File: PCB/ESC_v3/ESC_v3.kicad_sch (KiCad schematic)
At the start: 75 parts, among them J1 Conn_01x04_Pin, J11 Screw_Terminal_01x01, J2 Screw_Terminal_01x01, Q1 NTMFS2D1N08XT1G, Q2 NTMFS2D1N08XT1G, Q3 NTMFS2D1N08XT1G, Q4 NTMFS2D1N08XT1G, Q5 NTMFS2D1N08XT1G, Q6 NTMFS2D1N08XT1G, U1 SN65HVD232

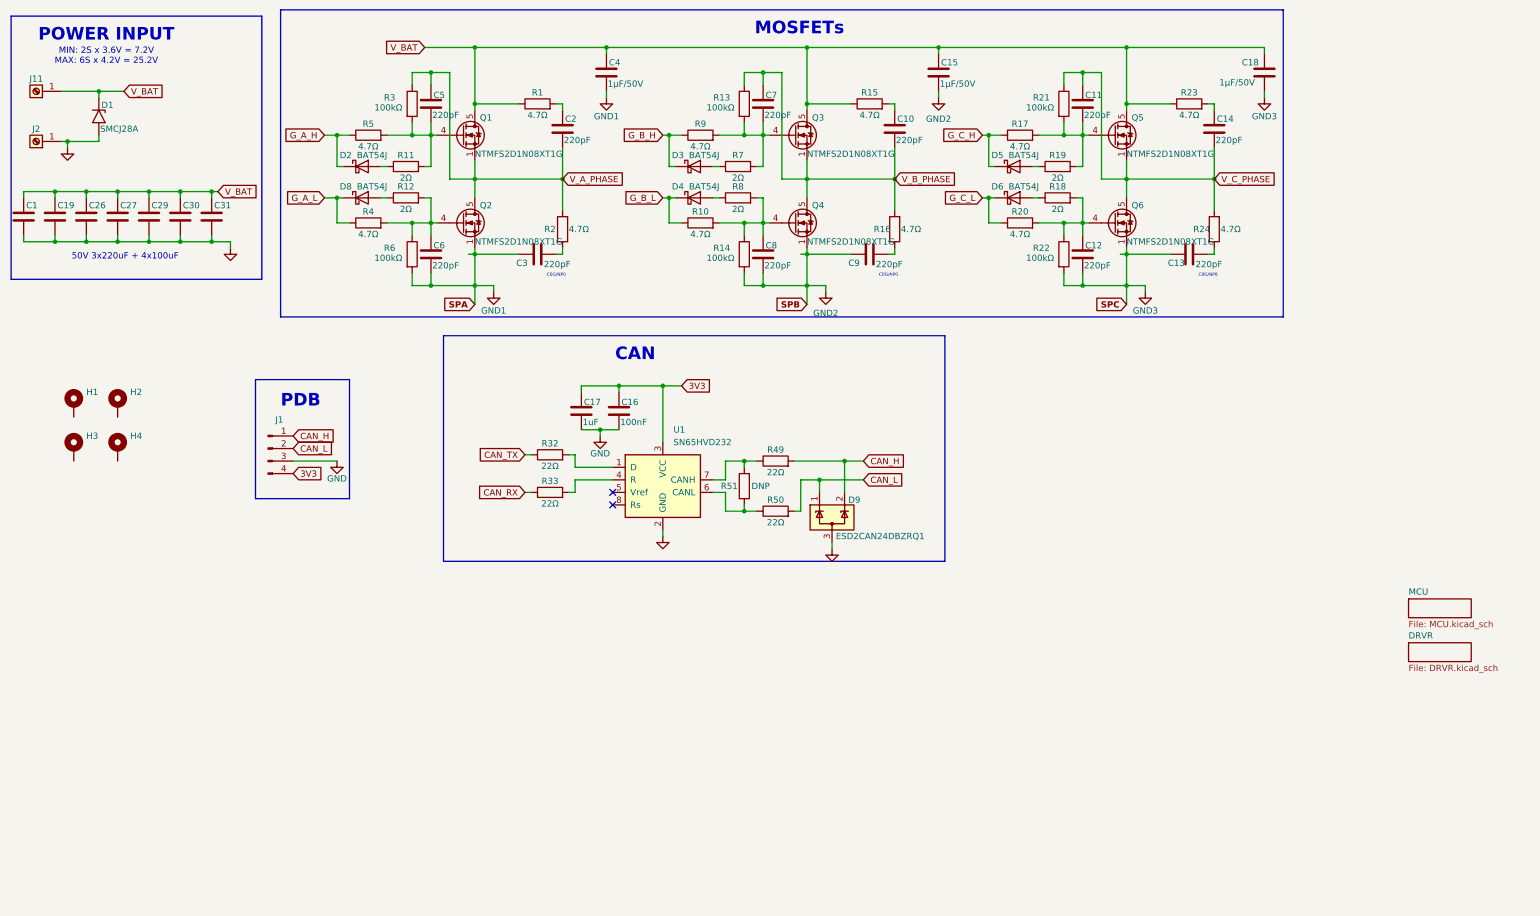
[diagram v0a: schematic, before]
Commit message: Update PCB layout and driver schematic
Adjust KiCad project files: many PCB footprint positions/rotations/uuids and silk/pad orientations updated, trace segments and widths adjusted, vias added/moved (several tented/free vias), and zone_connect enabled on referenced footprints. Correct MCU pin net assignments (PB4/PB5/PB6 / NFAULT / EN_DV) and other net fixes. In DRVR schematic change stroke styles to dashed and update a capacitor value from ">=10uF" to "22u". Remove several old backup zip files and add new backup snapshots. Miscellaneous small .kicad_prl/.kicad_sch/.ioc updates included for consistency and routing cleanup.
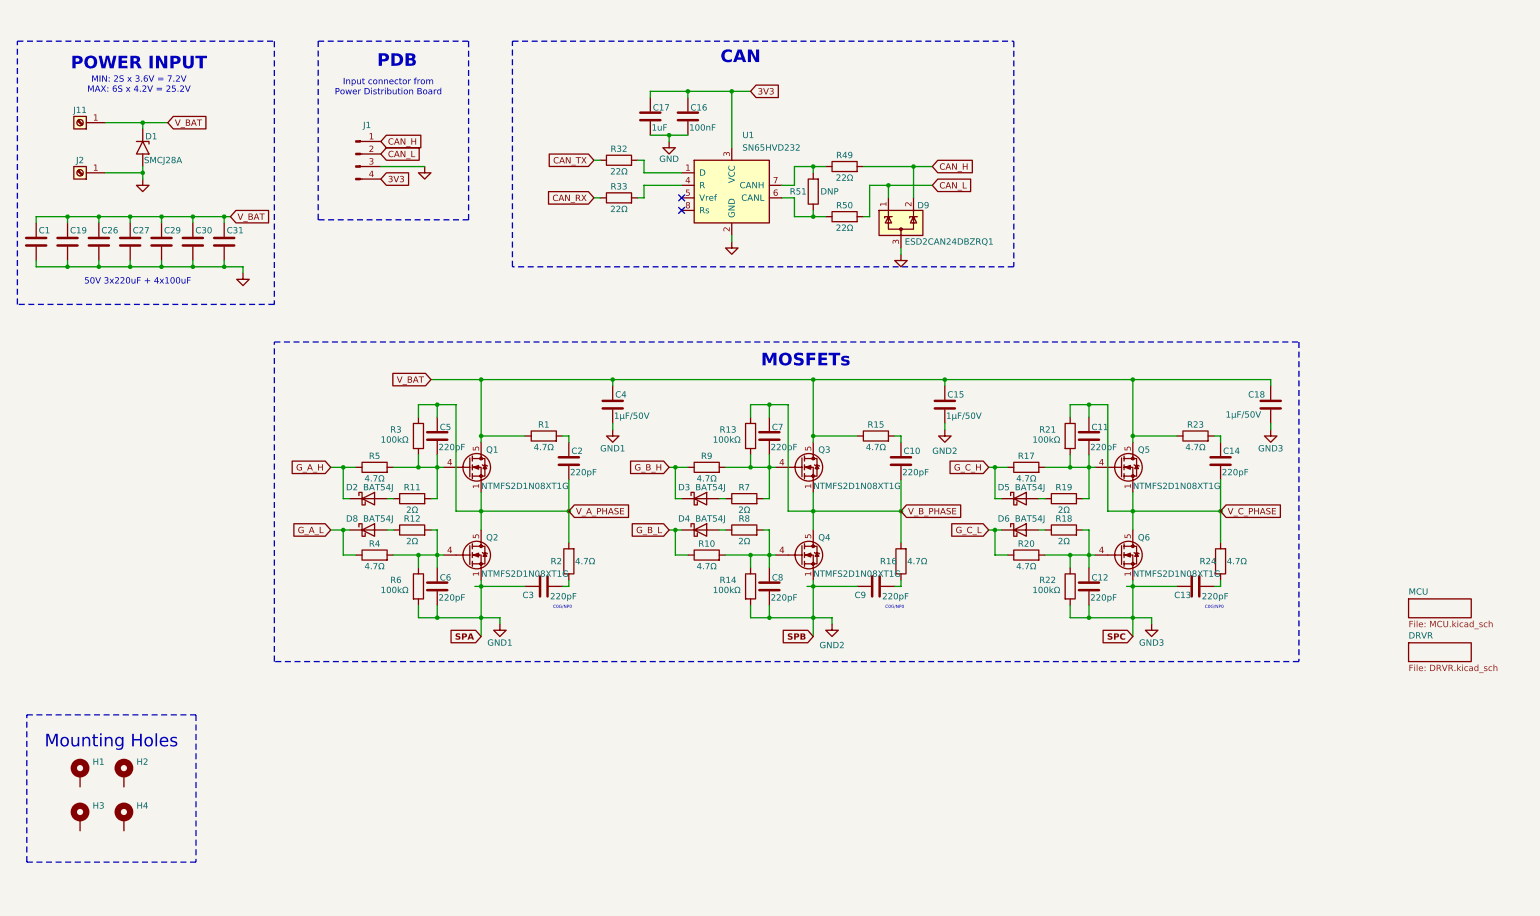
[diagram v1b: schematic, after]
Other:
- note added: "Input connector from Power Distribution Board"
- note added: "Mounting Holes"
- moved on the sheet: C1, C10, C11, C12, C13, C14, C15, C16, C17, C18, C19, C2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

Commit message: Reposition DRVR schematic elements
Adjust layout in PCB/ESC_v3/DRVR.kicad_sch: updated coordinates for rectangles, text labels, junctions, wires and pins to tidy and realign the driver schematic. Changes are graphical/coordinate-only (no netlist/electrical changes). Also touched project files (ESC_v3.*) and refreshed backup archives (deleted several older backups and added new snapshots).
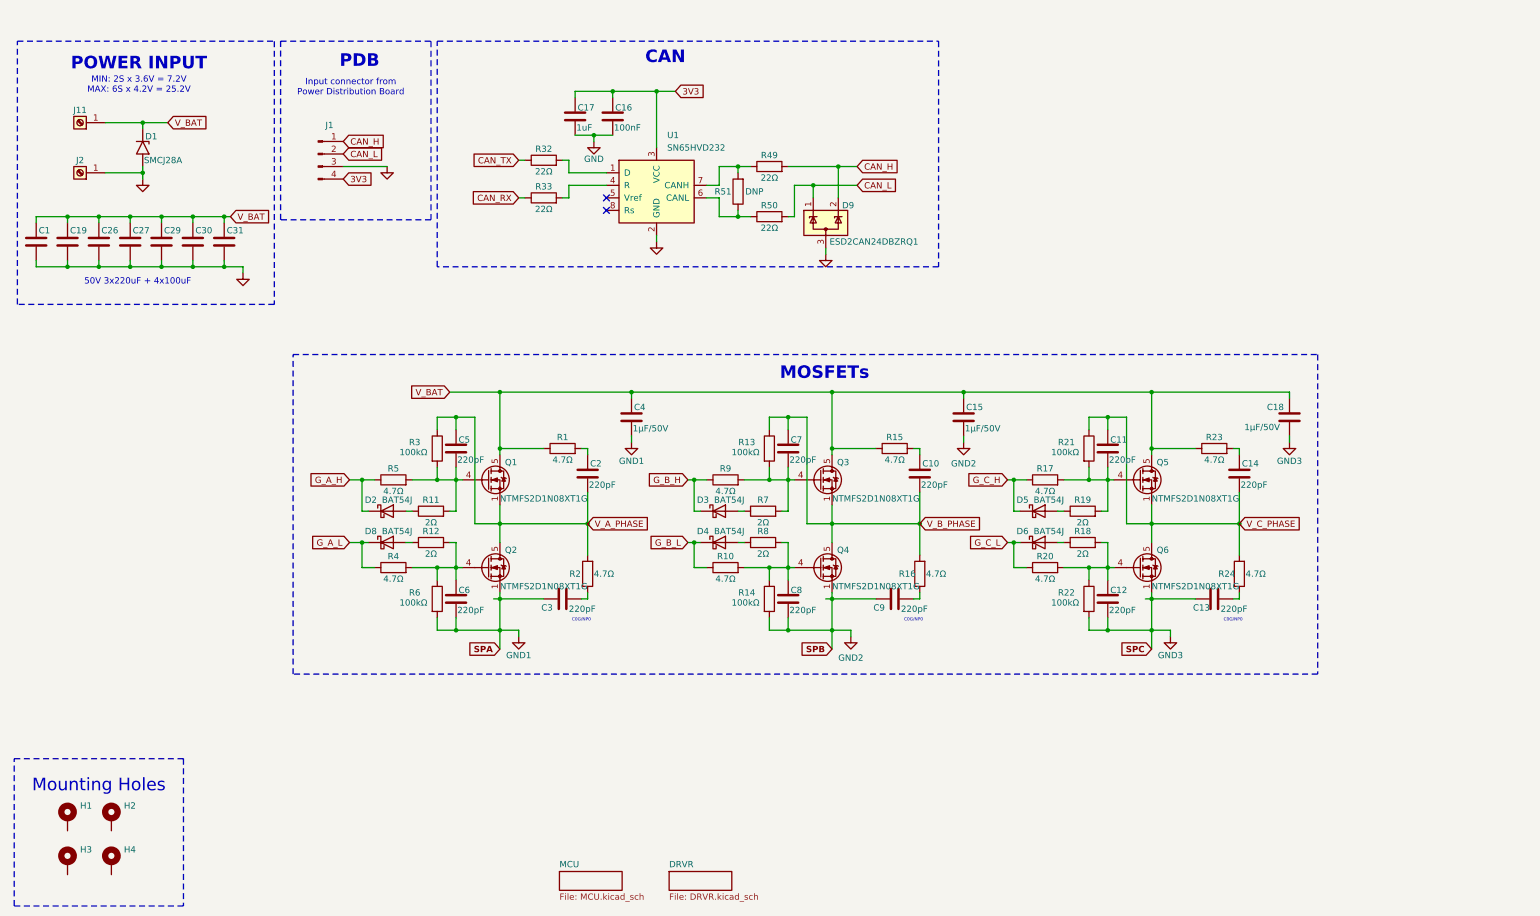
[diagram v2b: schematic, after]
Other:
- moved on the sheet: C10, C11, C12, C13, C14, C15, C16, C17, C18, C2, C3, C4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

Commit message: Update ESC_v3 schematics and PCB layout
Add net-tie symbol and +3V3/GND1 power symbols to DRVR schematic and reorganize schematic graphics (rectangles, text), junctions, and wires with updated coordinates/UUIDs. Also update top-level ESC_v3 schematic and MCU schematic along with PCB (.kicad_pcb) and panel (.kicad_prl) files. Remove several old backup zip files and add new backups for the ESC_v3 project.
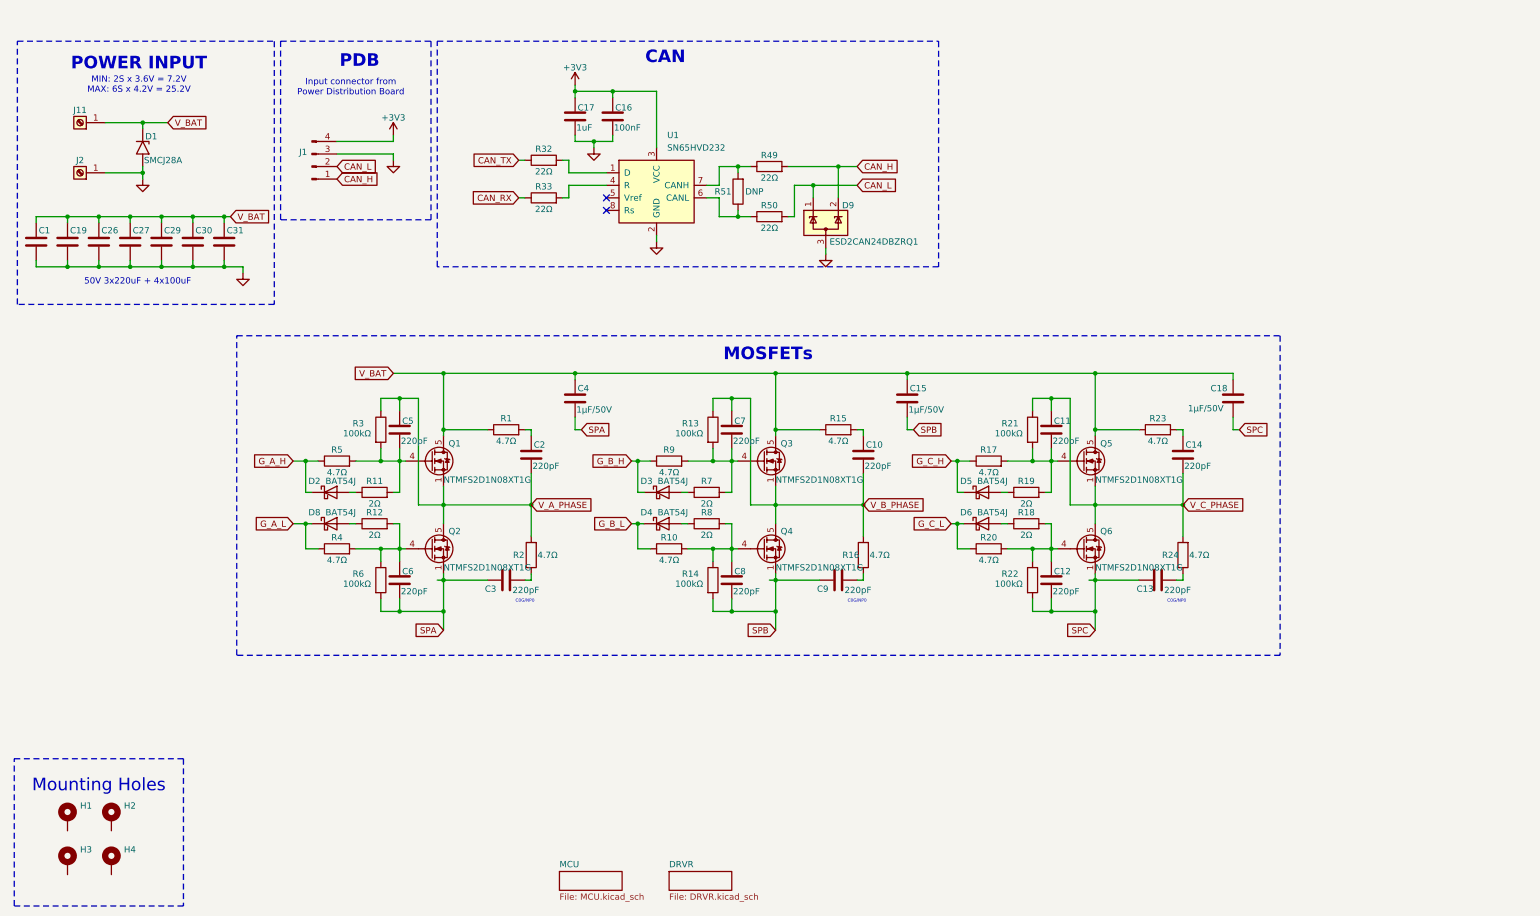
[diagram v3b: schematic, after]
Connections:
- net 3V3 renamed +3V3
- net GND1 renamed SPA
- net GND2 renamed SPB
- net GND3 renamed SPC
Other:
- moved on the sheet: C10, C11, C12, C13, C14, C15, C18, C2, C3, C4, C5, C6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

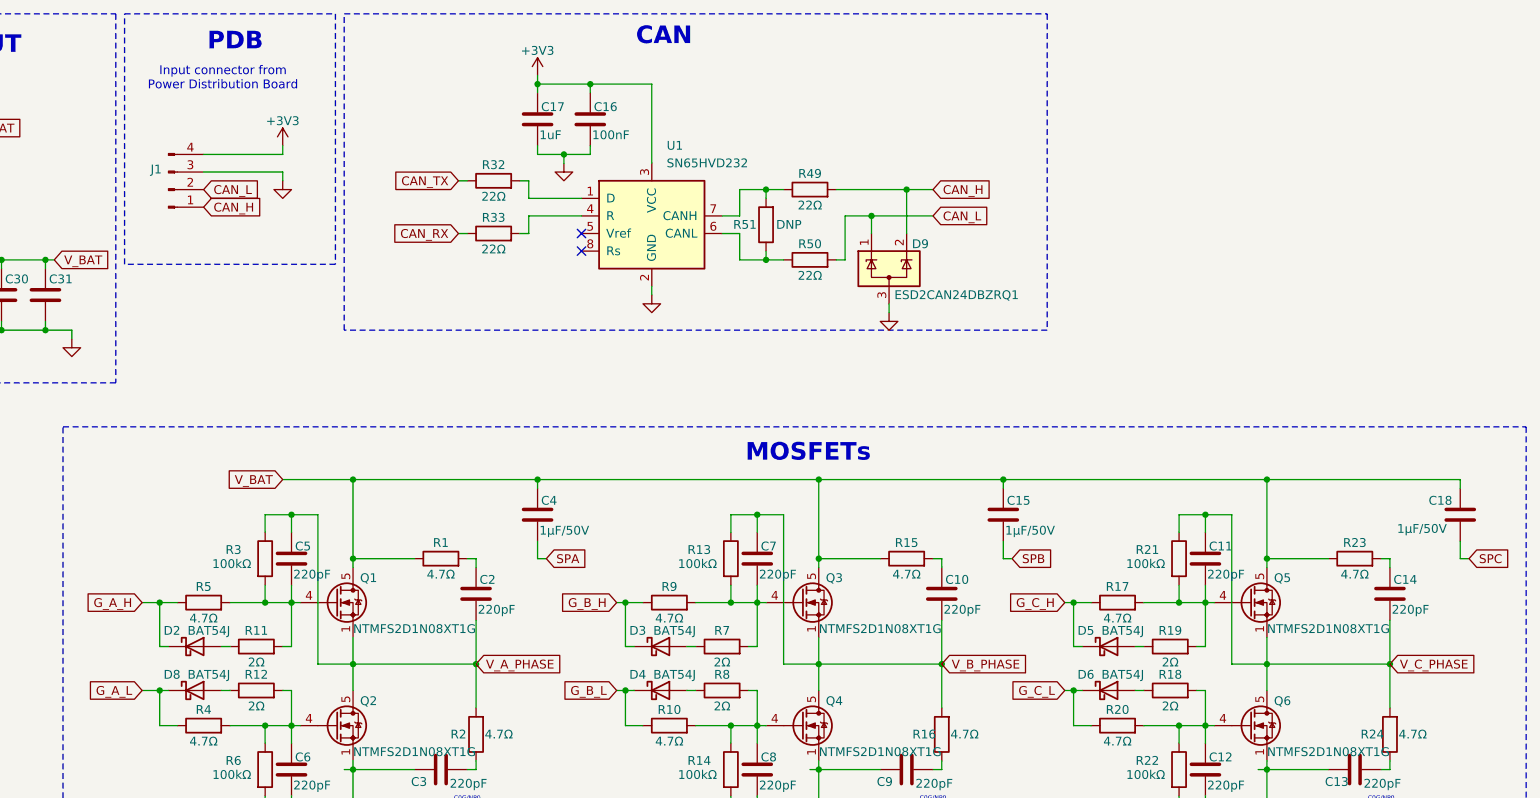
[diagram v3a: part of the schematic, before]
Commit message: Update DRVR schematic: relabels, wiring, net-ties
Refactor PCB/ESC_v3/DRVR.kicad_sch: cleaned up stray rectangles and comment text, repositioned many junctions and wires to fix connectivity, replaced/added global labels (reorganized SNA/SPA/SPB/SPC/SNB/SNC/etc.), and inserted NetTie symbols (NT1/NT3) with footprints to implement net ties. Updated symbol positions and UUIDs and removed obsolete schematic elements. Also touched top-level ESC_v3 files (ESC_v3.kicad_pcb, ESC_v3.kicad_prl, ESC_v3.kicad_sch, MCU.kicad_sch) and added/removed several backup archives.
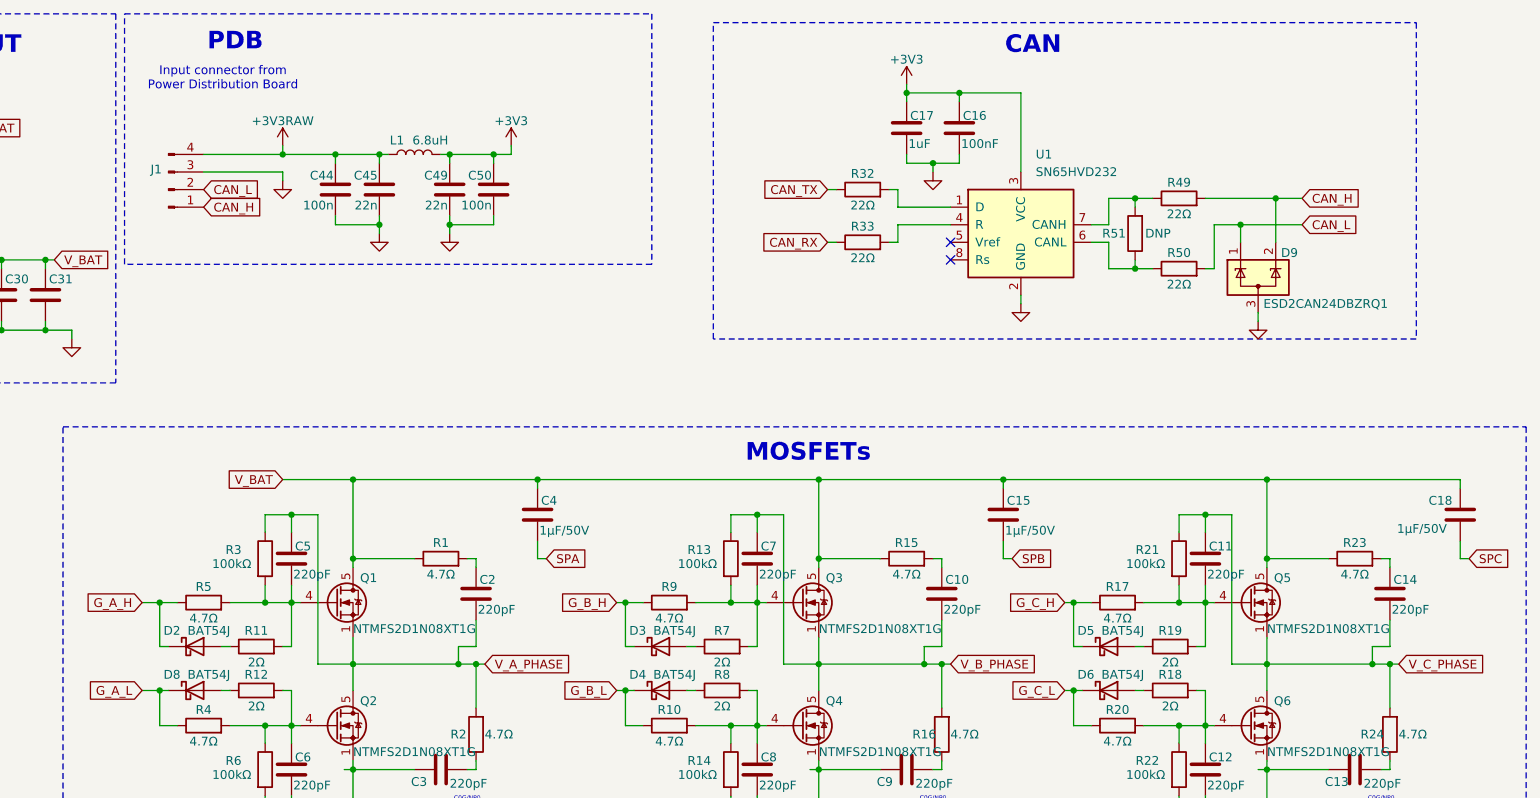
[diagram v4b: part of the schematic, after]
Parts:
- added C44, C50: 100n, Capacitor_SMD:C_0805_2012Metric, symbol Device:C
- added C45, C49: 22n, Capacitor_SMD:C_0805_2012Metric, symbol Device:C
- added L1: 6.8uH, Inductor_SMD:L_0805_2012Metric_Pad1.05x1.20mm_HandSolder, symbol Device:L
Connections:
- net +3V3: now also C49.2, C50.2, L1.2; no longer J1.4 (Pin_4)
- net GND: now also C44.1, C45.1, C49.1, C50.1
- new net +3V3RAW: C44.2, C45.2, J1.4 (Pin_4), L1.1
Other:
- moved on the sheet: C16, C17, D9, R32, R33, R49, R50, R51, U1
